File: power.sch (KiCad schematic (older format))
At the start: 57 parts, among them J11 Conn_02x05_Odd_Even, J2 PJ-002B, J4 Screw_Terminal_01x12, U11 LT3471, U12 LP38693MP-1.8, U13 LP38693MP-2.5, U14 LP38693MP-5.0, U17 LM2937xMP, U19 MAX6070BAUT21+T, U21 MC79M15_TO252, U5 LP38693MP-3.3

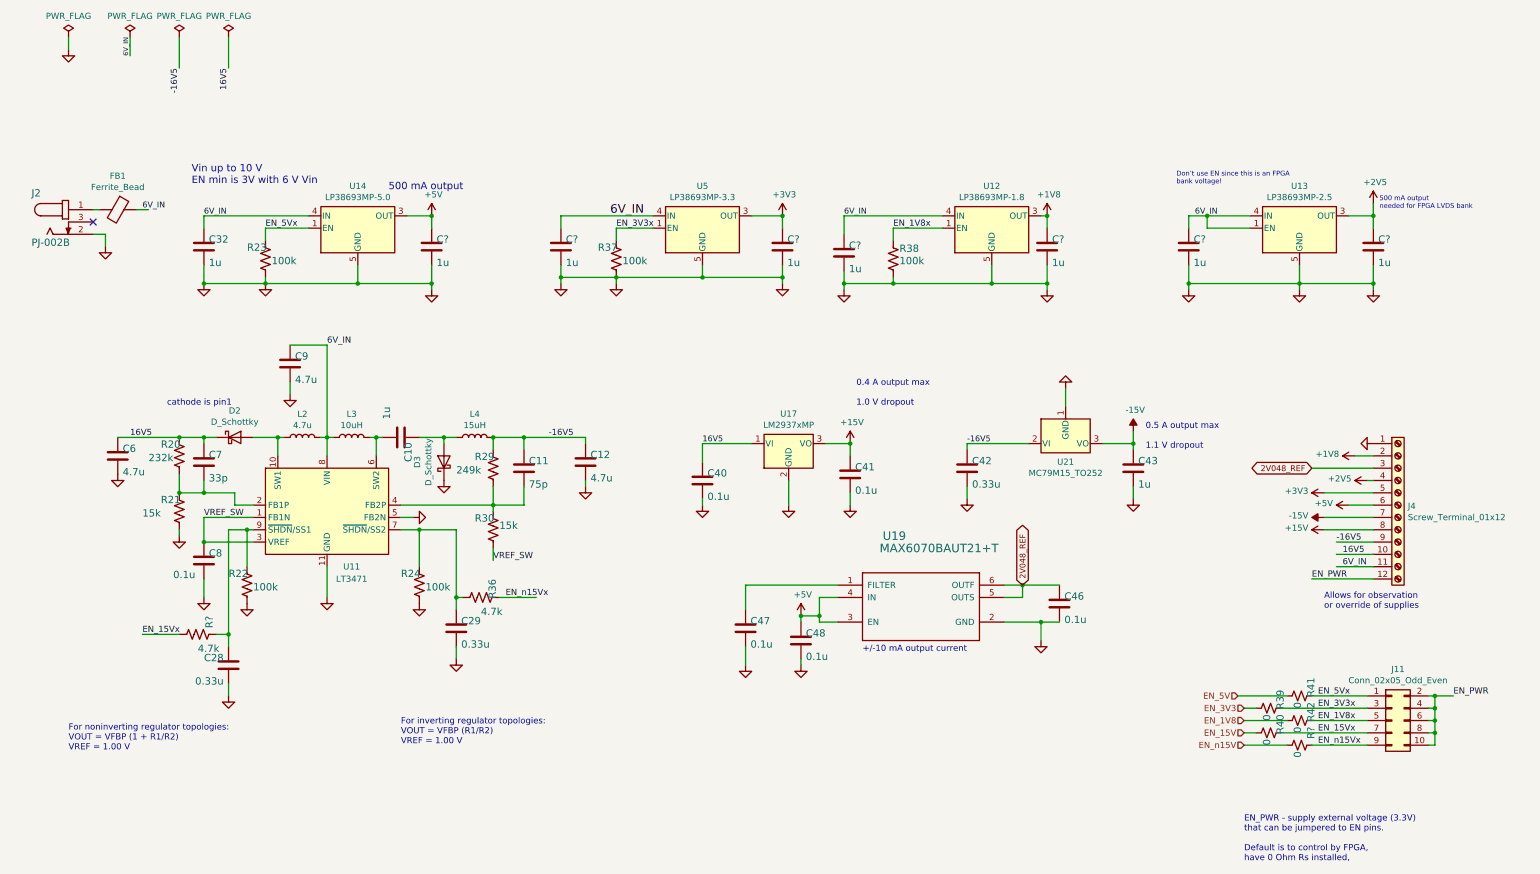
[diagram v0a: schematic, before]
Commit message: moved DCO 7960 signals to dedicated input clock routes
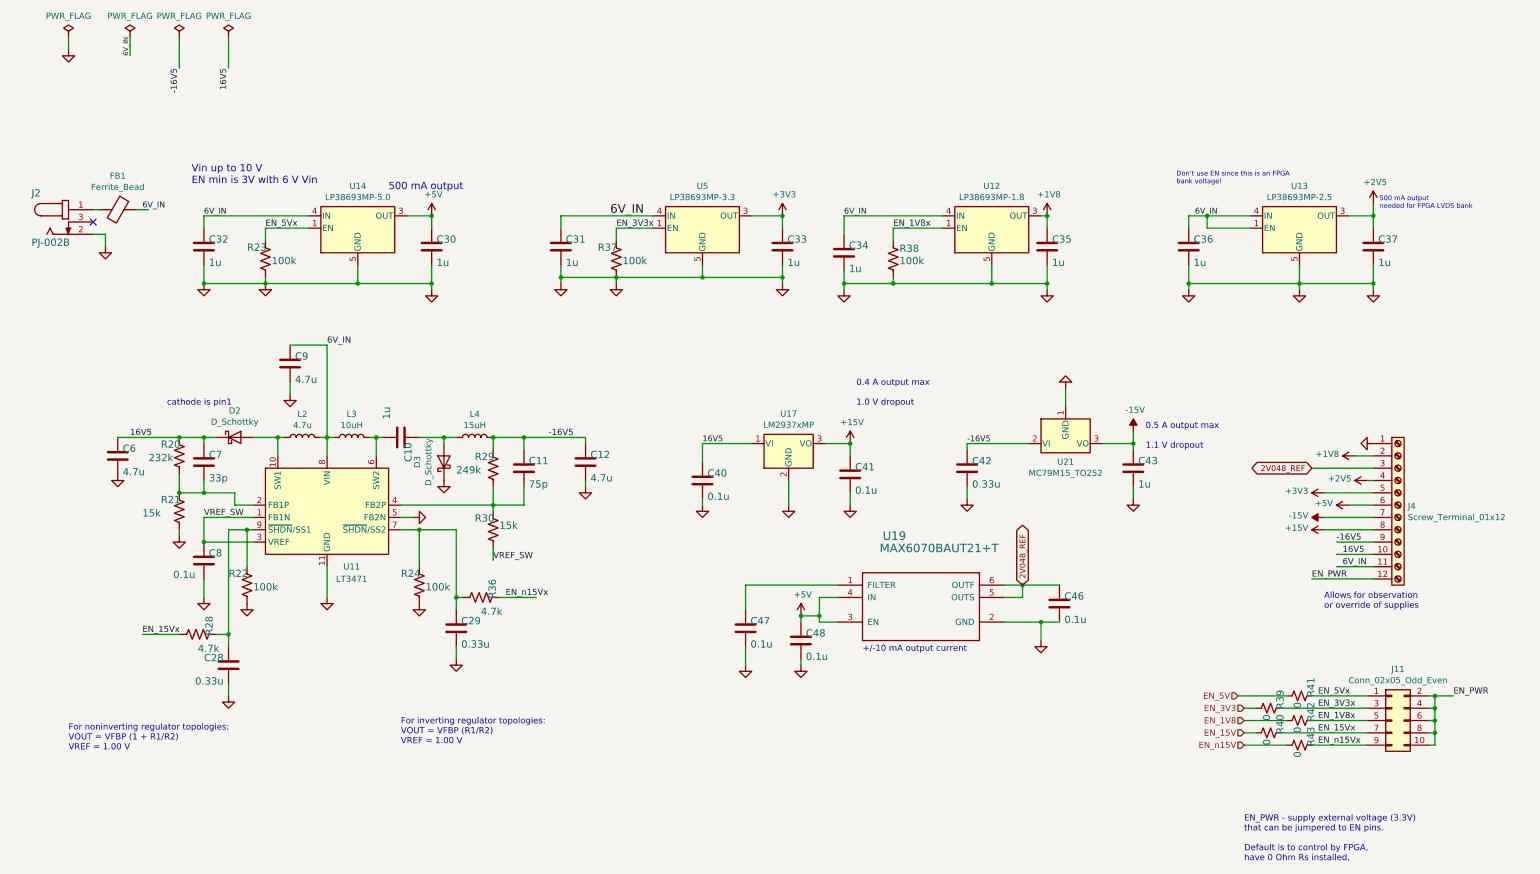
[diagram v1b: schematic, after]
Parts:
- gave numbers to parts that had none: 9
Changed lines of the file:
@@
 For inverting regulator topologies:\nVOUT = VFBP (R1/R2)\nVREF = 1.00 V
 $Comp
-L Device:R_US R?
+L Device:R_US R28
 U 1 1 60DE26F5
 P 1950 5700
-F 0 "R?" H 1800 5759 59  0000 L BNN
+F 0 "R28" H 1800 5759 59  0000 L BNN
 F 1 "4.7k" V 2100 5700 59  0000 L BNN
 F 2 "Resistor_SMD:R_0603_1608Metric" H 1950 5700 50  0001 C CNN
@@
 $EndComp
 $Comp
-L Device:R_Small_US R?
+L Device:R_Small_US R43
 U 1 1 60DE2F1F
 P 10900 6600
-F 0 "R?" H 10750 6659 59  0000 L BNN
+F 0 "R43" H 10750 6659 59  0000 L BNN
 F 1 "0" H 10950 6550 59  0000 L BNN
 F 2 "Resistor_SMD:R_0603_1608Metric" H 10900 6600 50  0001 C CNN
@@
 $EndComp
 $Comp
-L Device:C C?
+L Device:C C31
 U 1 1 60DE5C26
 P 4900 2550
-F 0 "C?" H 4940 2575 59  0000 L BNN
+F 0 "C31" H 4940 2575 59  0000 L BNN
 F 1 "1u" H 4940 2385 59  0000 L BNN
 F 2 "Capacitor_SMD:C_0603_1608Metric" H 4900 2550 50  0001 C CNN
@@
 $EndComp
 $Comp
-L Device:C C?
+L Device:C C30
 U 1 1 60DE60E5
 P 3850 2550
-F 0 "C?" H 3890 2575 59  0000 L BNN
+F 0 "C30" H 3890 2575 59  0000 L BNN
 F 1 "1u" H 3890 2385 59  0000 L BNN
 F 2 "Capacitor_SMD:C_0603_1608Metric" H 3850 2550 50  0001 C CNN
@@
 $EndComp
 $Comp
-L Device:C C?
+L Device:C C33
 U 1 1 60DE66AC
 P 6700 2550
-F 0 "C?" H 6740 2575 59  0000 L BNN
+F 0 "C33" H 6740 2575 59  0000 L BNN
 F 1 "1u" H 6740 2385 59  0000 L BNN
 F 2 "Capacitor_SMD:C_0603_1608Metric" H 6700 2550 50  0001 C CNN
@@
 $EndComp
 $Comp
-L Device:C C?
+L Device:C C34
 U 1 1 60DE6CB7
 P 7200 2600
-F 0 "C?" H 7240 2625 59  0000 L BNN
+F 0 "C34" H 7240 2625 59  0000 L BNN
 F 1 "1u" H 7240 2435 59  0000 L BNN
 F 2 "Capacitor_SMD:C_0603_1608Metric" H 7200 2600 50  0001 C CNN
@@
 $EndComp
 $Comp
-L Device:C C?
+L Device:C C35
 U 1 1 60DE7116
 P 8850 2550
-F 0 "C?" H 8890 2575 59  0000 L BNN
+F 0 "C35" H 8890 2575 59  0000 L BNN
 F 1 "1u" H 8890 2385 59  0000 L BNN
 F 2 "Capacitor_SMD:C_0603_1608Metric" H 8850 2550 50  0001 C CNN
@@
 $EndComp
 $Comp
-L Device:C C?
+L Device:C C36
 U 1 1 60DE75A5
 P 10000 2550
-F 0 "C?" H 10040 2575 59  0000 L BNN
+F 0 "C36" H 10040 2575 59  0000 L BNN
 F 1 "1u" H 10040 2385 59  0000 L BNN
 F 2 "Capacitor_SMD:C_0603_1608Metric" H 10000 2550 50  0001 C CNN
@@
 $EndComp
 $Comp
-L Device:C C?
+L Device:C C37
 U 1 1 60DE794C
 P 11500 2550
-F 0 "C?" H 11540 2575 59  0000 L BNN
+F 0 "C37" H 11540 2575 59  0000 L BNN
 F 1 "1u" H 11540 2385 59  0000 L BNN
 F 2 "Capacitor_SMD:C_0603_1608Metric" H 11500 2550 50  0001 C CNN

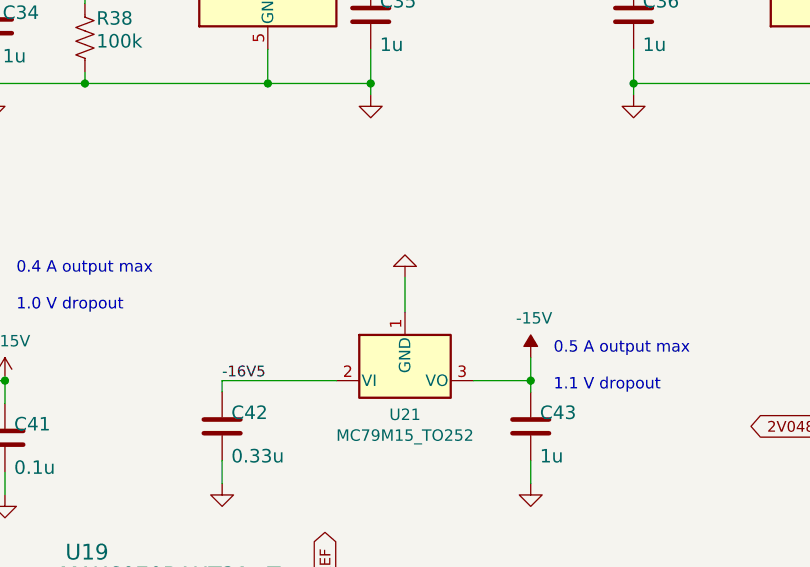
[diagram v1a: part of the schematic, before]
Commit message: added Unique ID chip
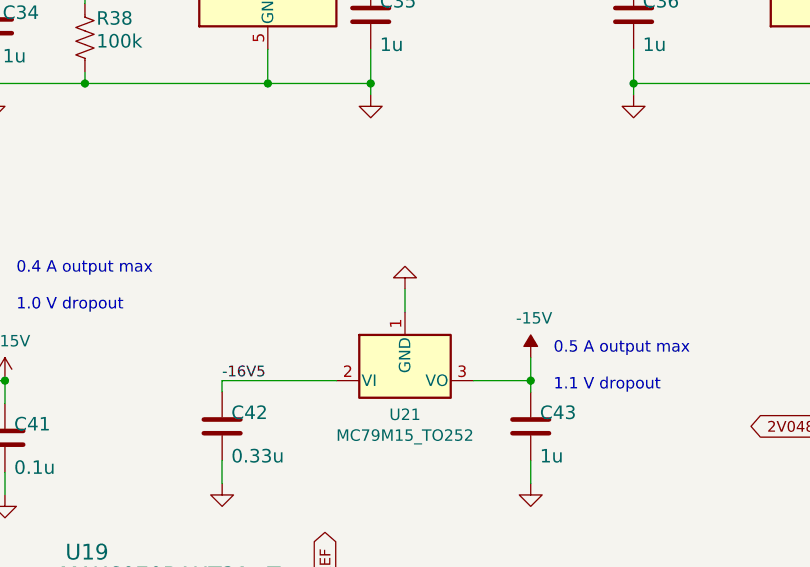
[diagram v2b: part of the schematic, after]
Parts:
- D3: footprint (none) -> Diode_SMD:D_Powermite2_AK
- J11: footprint (none) -> Connector_PinHeader_2.00mm:PinHeader_2x05_P2.00mm_Vertical_SMD; Manf# (none) -> 0877591064
- J4: footprint (none) -> TerminalBlock_Phoenix:TerminalBlock_Phoenix_MPT-0,5-12-2.54_1x12_P2.54mm_Horizontal; Manf# (none) -> OSTVN12A150
- L2: footprint (none) -> covg-kicad:SRR4018-4R7Y; Manf# CDRH3D16/HPNP-100MC -> SRR4018-4R7Y
- L3: footprint (none) -> covg-kicad:NRS5020T100MMGJ; Manf# CDRH3D16/HPNP-100MC -> NRS5020T100MMGJ
- L4: footprint (none) -> covg-kicad:SRR6028-150Y; Manf# CDRH3D16/HPNP-100MC -> SRR6028-150Y‎
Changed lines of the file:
@@
 F 0 "L2" V 2990 4100 50  0000 C CNN
 F 1 "4.7u" V 2899 4100 50  0000 C CNN
-F 2 "" H 2800 4100 50  0001 C CNN
+F 2 "covg-kicad:SRR4018-4R7Y" H 2800 4100 50  0001 C CNN
 F 3 "~" H 2800 4100 50  0001 C CNN
-F 4 "CDRH3D16/HPNP-100MC" V 2800 4100 50  0001 C CNN "Manf#"
+F 4 "SRR4018-4R7Y" V 2800 4100 50  0001 C CNN "Manf#"
 	1    2800 4100
 	0    -1   -1   0
@@
 F 0 "L3" V 3390 4100 50  0000 C CNN
 F 1 "10uH" V 3299 4100 50  0000 C CNN
-F 2 "" H 3200 4100 50  0001 C CNN
+F 2 "covg-kicad:NRS5020T100MMGJ" H 3200 4100 50  0001 C CNN
 F 3 "~" H 3200 4100 50  0001 C CNN
-F 4 "CDRH3D16/HPNP-100MC" V 3200 4100 50  0001 C CNN "Manf#"
+F 4 "NRS5020T100MMGJ" V 3200 4100 50  0001 C CNN "Manf#"
 	1    3200 4100
 	0    -1   -1   0
@@
 F 0 "D3" H 3950 4517 50  0000 C CNN
 F 1 "D_Schottky" H 3950 4426 50  0000 C CNN
-F 2 "" H 3950 4300 50  0001 C CNN
+F 2 "Diode_SMD:D_Powermite2_AK" H 3950 4300 50  0001 C CNN
 F 3 "~" H 3950 4300 50  0001 C CNN
 F 4 "B0540W" H 3950 4300 50  0001 C CNN "Manf#"
@@
 F 0 "L4" V 4390 4100 50  0000 C CNN
 F 1 "15uH" V 4299 4100 50  0000 C CNN
-F 2 "" H 4200 4100 50  0001 C CNN
+F 2 "covg-kicad:SRR6028-150Y" H 4200 4100 50  0001 C CNN
 F 3 "~" H 4200 4100 50  0001 C CNN
-F 4 "CDRH3D16/HPNP-100MC" V 4200 4100 50  0001 C CNN "Manf#"
+F 4 "SRR6028-150Y‎" V 4200 4100 50  0001 C CNN "Manf#"
 	1    4200 4100
 	0    -1   -1   0
@@
 L power:GND #GND0112
 U 1 1 61491353
-P 9000 3700
-F 0 "#GND0112" H 9000 3700 50  0001 C CNN
-F 1 "GND" H 8900 3600 59  0001 L BNN
-F 2 "" H 9000 3700 50  0001 C CNN
-F 3 "" H 9000 3700 50  0001 C CNN
-	1    9000 3700
+P 9000 3750
+F 0 "#GND0112" H 9000 3750 50  0001 C CNN
+F 1 "GND" H 8900 3650 59  0001 L BNN
+F 2 "" H 9000 3750 50  0001 C CNN
+F 3 "" H 9000 3750 50  0001 C CNN
+	1    9000 3750
 	-1   0    0    1
 $EndComp
@@
 F 0 "J4" H 11780 4642 50  0000 L CNN
 F 1 "Screw_Terminal_01x12" H 11780 4551 50  0000 L CNN
-F 2 "" H 11700 4650 50  0001 C CNN
+F 2 "TerminalBlock_Phoenix:TerminalBlock_Phoenix_MPT-0,5-12-2.54_1x12_P2.54mm_Horizontal" H 11700 4650 50  0001 C CNN
 F 3 "~" H 11700 4650 50  0001 C CNN
+F 4 "OSTVN12A150" H 11700 4650 50  0001 C CNN "Manf#"
 	1    11700 4650
 	1    0    0    -1
@@
 F 0 "J11" H 11700 6817 50  0000 C CNN
 F 1 "Conn_02x05_Odd_Even" H 11700 6726 50  0000 C CNN
-F 2 "" H 11650 6400 50  0001 C CNN
+F 2 "Connector_PinHeader_2.00mm:PinHeader_2x05_P2.00mm_Vertical_SMD" H 11650 6400 50  0001 C CNN
 F 3 "~" H 11650 6400 50  0001 C CNN
+F 4 "0877591064" H 11650 6400 50  0001 C CNN "Manf#"
 	1    11650 6400
 	1    0    0    -1
@@
 	9300 4150 9550 4150
 Wire Wire Line
-	9000 3700 9000 3850
+	9000 3750 9000 3850
 Wire Wire Line
 	3250 2850 3850 2850

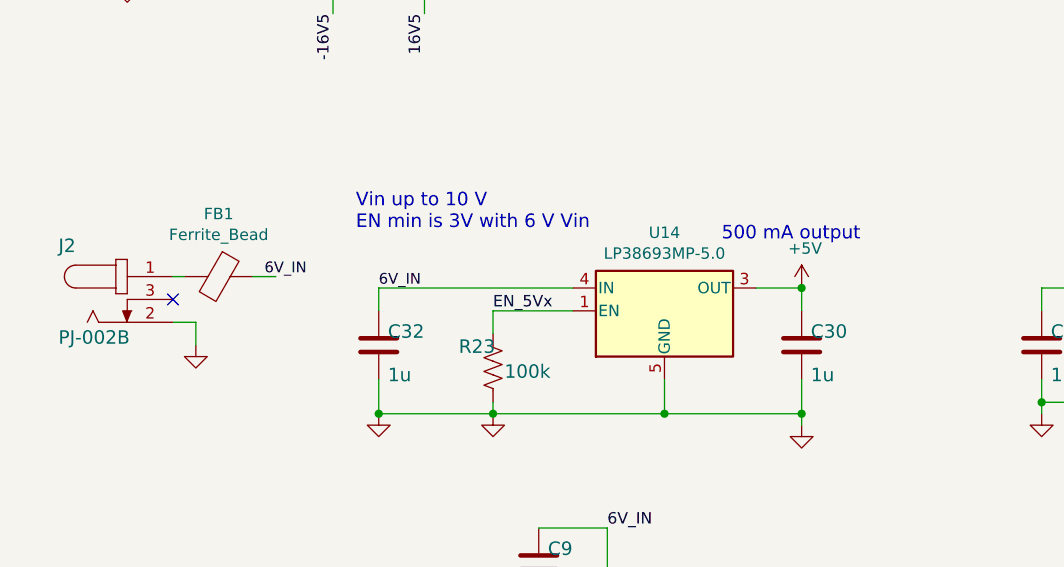
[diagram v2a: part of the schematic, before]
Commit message: layout cleanup; removed custom footrpints
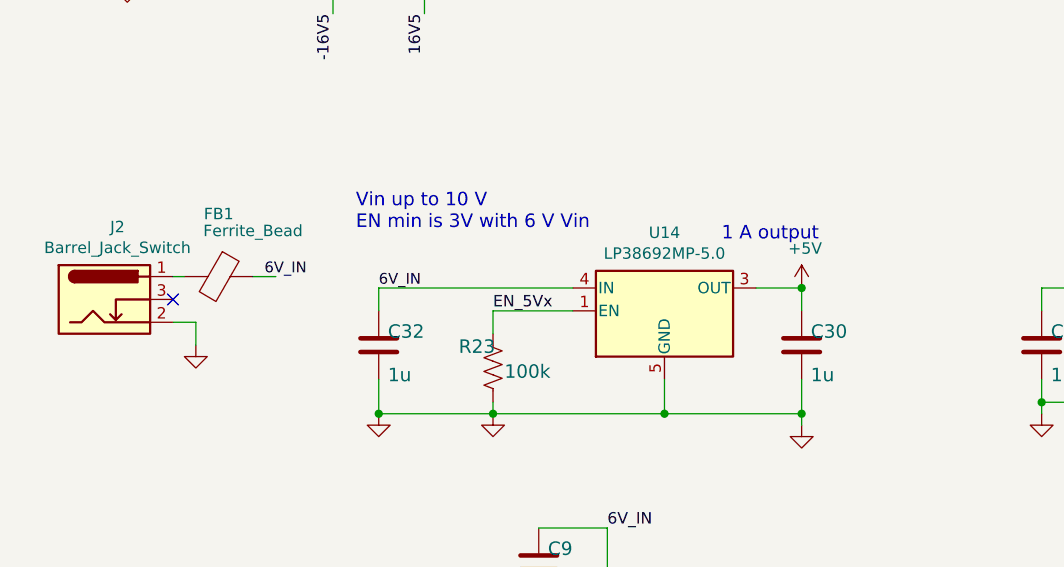
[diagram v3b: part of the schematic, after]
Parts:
- removed J2: PJ-002B, adc_dac_v1:CUI_PJ-002B, symbol adc_dac_v1-eagle-import:PJ-002B
- added J2: Barrel_Jack_Switch, covg-kicad:CUI_PJ-002B, symbol Connector:Barrel_Jack_Switch
- U14: value LP38693MP-5.0 -> LP38692MP-5.0; Manf# LP38693MP-5.0/NOPB -> LP38692MPX-5.0/NOPB; Notes (none) -> LP38693 is 500 mA version. LP38692 is 1 A version. Footprin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
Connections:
- net GND: now also J2.2
- net at FB1.2: now also J2.1
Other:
- note added: "1 A output"
- note removed: "500 mA output"
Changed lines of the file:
@@
-$EndComp
-$Comp
-L adc_dac_v1-eagle-import:PJ-002B J2
-U 1 1 F1780596
-P 900 2350
-F 0 "J2" H 599 2550 59  0000 L BNN
-F 1 "PJ-002B" H 599 2149 59  0000 L BNN
-F 2 "adc_dac_v1:CUI_PJ-002B" H 900 2350 50  0001 C CNN
-F 3 "" H 900 2350 50  0001 C CNN
-F 4 "PJ-002B" H 599 2650 50  0001 C CNN "Manf#"
-	1    900  2350
-	1    0    0    -1
 $EndComp
 $Comp
@@
 P 3250 2400
 F 0 "U14" H 3250 2742 50  0000 C CNN
-F 1 "LP38693MP-5.0" H 3250 2651 50  0000 C CNN
+F 1 "LP38692MP-5.0" H 3250 2651 50  0000 C CNN
 F 2 "Package_TO_SOT_SMD:SOT-223-5" H 3250 2400 50  0001 C CNN
 F 3 "https://www.ti.com/lit/ds/symlink/lp38693.pdf" H 3250 2400 50  0001 C CNN
-F 4 "LP38693MP-5.0/NOPB" H 3250 2400 50  0001 C CNN "Manf#"
+F 4 "LP38692MPX-5.0/NOPB" H 3250 2400 50  0001 C CNN "Manf#"
+F 5 "LP38693 is 500 mA version. LP38692 is 1 A version. Footprints are the same." H 3250 2400 50  0001 C CNN "Notes"
 	1    3250 2400
 	1    0    0    -1
@@
 P 1300 2250
 F 0 "FB1" V 1026 2250 50  0000 C CNN
-F 1 "Ferrite_Bead" V 1117 2250 50  0000 C CNN
+F 1 "Ferrite_Bead" V 1100 2400 50  0000 C CNN
 F 2 "Capacitor_SMD:C_1206_3216Metric" V 1230 2250 50  0001 C CNN
 F 3 "~" H 1300 2250 50  0001 C CNN
@@
 2V048_REF
 Text Notes 3500 2100 0    59   ~ 0
-500 mA output
+1 A output
 Text Label 3000 3350 0    50   ~ 0
 6V_IN
@@
 	1    0    0    -1
 $EndComp
+$Comp
+L Connector:Barrel_Jack_Switch J2
+U 1 1 60DCC1A2
+P 800 2350
+F 0 "J2" H 857 2667 50  0000 C CNN
+F 1 "Barrel_Jack_Switch" H 857 2576 50  0000 C CNN
+F 2 "covg-kicad:CUI_PJ-002B" H 850 2310 50  0001 C CNN
+F 3 "~" H 850 2310 50  0001 C CNN
+F 4 "PJ-002B" H 800 2350 50  0001 C CNN "Manf#"
+	1    800  2350
+	1    0    0    -1
+$EndComp
